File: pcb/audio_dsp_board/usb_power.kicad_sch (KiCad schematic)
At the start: 14 parts, among them J4 USB_C_Receptacle_USB2.0_14P, U3 AMS1117-3.3, U4 AMS1117-3.3, U5 AMS1117-1.5

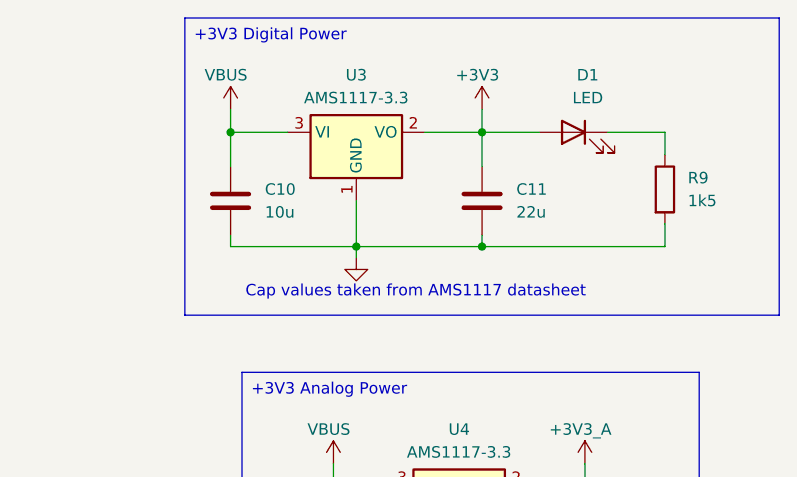
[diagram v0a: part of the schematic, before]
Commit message: Schematic capture, placement, routing complete
Sending board to JLCPCB for manufacturing and assembly.
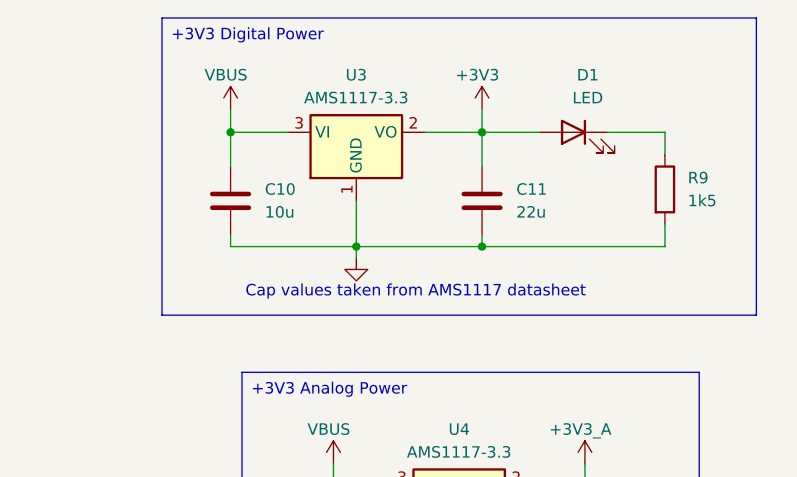
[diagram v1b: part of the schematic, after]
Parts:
- C10, C26, C28: footprint Capacitor_SMD:C_0402_1005Metric -> Capacitor_SMD:C_0603_1608Metric
- C11, C27, C29: footprint Capacitor_SMD:C_0402_1005Metric -> Capacitor_SMD:C_0805_2012Metric
- D1: footprint (none) -> Diode_SMD:D_0603_1608Metric
- J4: footprint (none) -> Connector_USB:USB_C_Receptacle_XKB_U262-16XN-4BVC11
- R4, R5, R9: footprint (none) -> Resistor_SMD:R_0402_1005Metric
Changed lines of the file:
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@@
 	(text_box "+3V3 Digital Power"
 		(exclude_from_sim no)
-		(at 167.64 46.99 0)
+		(at 165.1 46.99 0)
 		(size 66.04 33.02)
 		(stroke
@@
 			)
 		)
-		(property "Footprint" ""
+		(property "Footprint" "Resistor_SMD:R_0402_1005Metric"
 			(at 130.048 90.17 90)
 			(effects
@@
 			)
 		)
-		(property "Footprint" ""
+		(property "Footprint" "Resistor_SMD:R_0402_1005Metric"
 			(at 219.202 66.04 90)
 			(effects
@@
 			)
 		)
-		(property "Footprint" ""
+		(property "Footprint" "Resistor_SMD:R_0402_1005Metric"
 			(at 119.888 90.17 90)
 			(effects
@@
 			)
 		)
-		(property "Footprint" "Capacitor_SMD:C_0402_1005Metric"
+		(property "Footprint" "Capacitor_SMD:C_0603_1608Metric"
 			(at 186.3852 148.59 0)
 			(effects
@@
 			)
 		)
-		(property "Footprint" "Capacitor_SMD:C_0402_1005Metric"
+		(property "Footprint" "Capacitor_SMD:C_0603_1608Metric"
 			(at 173.6852 71.12 0)
 			(effects
@@
 			)
 		)
-		(property "Footprint" "Capacitor_SMD:C_0402_1005Metric"
+		(property "Footprint" "Capacitor_SMD:C_0805_2012Metric"
 			(at 201.6252 71.12 0)
 			(effects
@@
 			)
 		)
-		(property "Footprint" ""
+		(property "Footprint" "Connector_USB:USB_C_Receptacle_XKB_U262-16XN-4BVC11"
 			(at 77.47 92.71 0)
 			(effects
@@
 			)
 		)
-		(property "Footprint" "Capacitor_SMD:C_0402_1005Metric"
+		(property "Footprint" "Capacitor_SMD:C_0805_2012Metric"
 			(at 213.0552 110.49 0)
 			(effects
@@
 			)
 		)
-		(property "Footprint" ""
+		(property "Footprint" "Diode_SMD:D_0603_1608Metric"
 			(at 210.82 59.69 0)
 			(effects
@@
 			)
 		)
-		(property "Footprint" "Capacitor_SMD:C_0402_1005Metric"
+		(property "Footprint" "Capacitor_SMD:C_0805_2012Metric"
 			(at 214.3252 148.59 0)
 			(effects
@@
 			)
 		)
-		(property "Footprint" "Capacitor_SMD:C_0402_1005Metric"
+		(property "Footprint" "Capacitor_SMD:C_0603_1608Metric"
 			(at 185.1152 110.49 0)
 			(effects
